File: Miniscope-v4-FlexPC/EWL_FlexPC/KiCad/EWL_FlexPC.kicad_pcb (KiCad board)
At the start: 2 copper layers, 14.6 x 14.5 mm, 0 parts

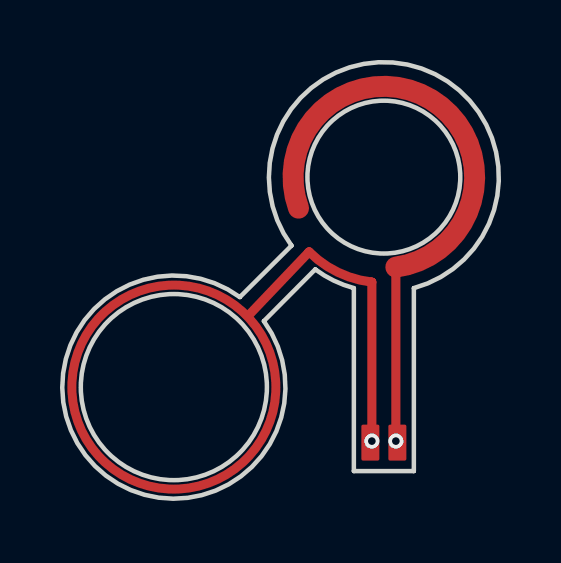
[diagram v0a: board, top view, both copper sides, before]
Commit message: Extend EWL FlexPC by 1mm
This should be the final design for the V4 EWL FlexPC connector. This commit adds 1mm to the length of flexPC that gets soldered to the LED/EWL PCB. This gives a bit more slack to the FlexPC to make soldering and assembly easier.
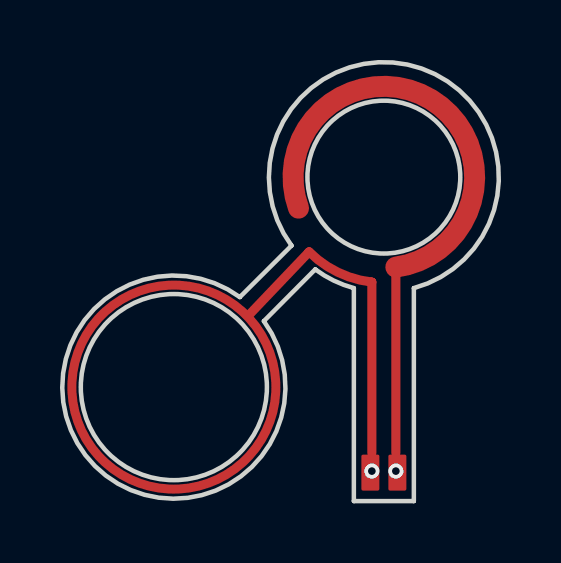
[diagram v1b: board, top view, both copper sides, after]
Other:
- board size 14.6 x 14.5 mm -> 14.6 x 14.6 mm
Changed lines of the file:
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@@
     (solder_mask_min_width 0.25)
     (aux_axis_origin 0 0)
-    (visible_elements FFFFFF7F)
+    (visible_elements 7FFFFFFF)
     (pcbplotparams
       (layerselection 0x010fc_ffffffff)
@@
     (uvia_drill 0.1)
   )
-  (gr_circle (center 49.6 38.8) (end 49.727 38.8) (layer B.Mask) (width 0.254))
-  (gr_circle (center 50.4 38.8) (end 50.527 38.8) (layer B.Mask) (width 0.254))
+  (gr_circle (center 49.6 39.8) (end 49.727 39.8) (layer B.Mask) (width 0.254))
+  (gr_circle (center 50.4 39.8) (end 50.527 39.8) (layer B.Mask) (width 0.254))
   (gr_arc (start 50 30) (end 49.6 33.5) (angle 38.48019825) (layer F.Cu) (width 0.3048))
   (gr_line (start 47.509016 32.490984) (end 45.5 34.6) (layer F.Cu) (width 0.3048))
-  (gr_poly (pts (xy 49.3 38.3) (xy 49.3 39.3) (xy 49.3 39.4) (xy 49.8 39.4) (xy 49.8 38.3)) (layer F.Mask) (width 0.1))
-  (gr_poly (pts (xy 49.3 38.3) (xy 49.3 39.3) (xy 49.3 39.4) (xy 49.8 39.4) (xy 49.8 38.3)) (layer F.Cu) (width 0.1))
+  (gr_poly (pts (xy 49.3 39.3) (xy 49.3 40.3) (xy 49.3 40.4) (xy 49.8 40.4) (xy 49.8 39.3)) (layer F.Mask) (width 0.1))
+  (gr_poly (pts (xy 49.3 39.3) (xy 49.3 40.3) (xy 49.3 40.4) (xy 49.8 40.4) (xy 49.8 39.3)) (layer F.Cu) (width 0.1))
   (gr_circle (center 43 37) (end 43.1 40.1) (layer Edge.Cuts) (width 0.15))
-  (gr_poly (pts (xy 50.2 38.3) (xy 50.2 39.3) (xy 50.2 39.4) (xy 50.7 39.4) (xy 50.7 38.3)) (layer F.Cu) (width 0.1))
-  (gr_poly (pts (xy 50.2 38.3) (xy 50.2 39.3) (xy 50.2 39.4) (xy 50.7 39.4) (xy 50.7 38.3)) (layer F.Mask) (width 0.1))
+  (gr_poly (pts (xy 50.2 39.3) (xy 50.2 40.3) (xy 50.2 40.4) (xy 50.7 40.4) (xy 50.7 39.3)) (layer F.Cu) (width 0.1))
+  (gr_poly (pts (xy 50.2 39.3) (xy 50.2 40.3) (xy 50.2 40.4) (xy 50.7 40.4) (xy 50.7 39.3)) (layer F.Mask) (width 0.1))
   (gr_circle (center 43 37) (end 46.5 37) (layer F.Mask) (width 0.5))
   (gr_line (start 50.4 39.2) (end 50.4 33) (layer F.Cu) (width 0.3048))
@@
   (gr_arc (start 50 30) (end 50.999999 33.699999) (angle -291.4490342) (layer Edge.Cuts) (width 0.15))
   (gr_circle (center 50 30) (end 52.5476 30) (layer Edge.Cuts) (width 0.15))
-  (gr_line (start 51 39.8) (end 51 33.7) (layer Edge.Cuts) (width 0.15))
+  (gr_line (start 51 40.8) (end 51 33.7) (layer Edge.Cuts) (width 0.15))
   (gr_arc (start 50 30) (end 50.4 33) (angle -282.4053422) (layer F.Cu) (width 0.7))
   (gr_line (start 47.713529 33.076043) (end 45.999999 34.800001) (layer Edge.Cuts) (width 0.15))
-  (gr_line (start 49 39.8) (end 49 33.7) (layer Edge.Cuts) (width 0.15))
+  (gr_line (start 49 40.8) (end 49 33.7) (layer Edge.Cuts) (width 0.15))
   (gr_line (start 46.921924 32.283734) (end 45.2 34) (layer Edge.Cuts) (width 0.15))
-  (gr_line (start 49 39.8) (end 51 39.8) (layer Edge.Cuts) (width 0.15))
+  (gr_line (start 49 40.8) (end 51 40.8) (layer Edge.Cuts) (width 0.15))
   (gr_circle (center 50 30) (end 52.925 30) (layer F.Mask) (width 0.45))
   (gr_arc (start 43 37) (end 45.199999 34.000001) (angle -342.5076755) (layer Edge.Cuts) (width 0.15))
   (gr_arc (start 50 30) (end 49.000001 33.699999) (angle 21.5) (layer Edge.Cuts) (width 0.15))
-  (via (at 50.4 38.8) (size 0.508) (drill 0.254) (layers F.Cu B.Cu) (net 0))
-  (via (at 49.6 38.8) (size 0.508) (drill 0.254) (layers F.Cu B.Cu) (net 0))
+  (via (at 50.4 39.8) (size 0.508) (drill 0.254) (layers F.Cu B.Cu) (net 0))
+  (via (at 49.6 39.8) (size 0.508) (drill 0.254) (layers F.Cu B.Cu) (net 0))
 )
